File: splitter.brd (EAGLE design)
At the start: 23.8 x 17.8 mm, 16 parts

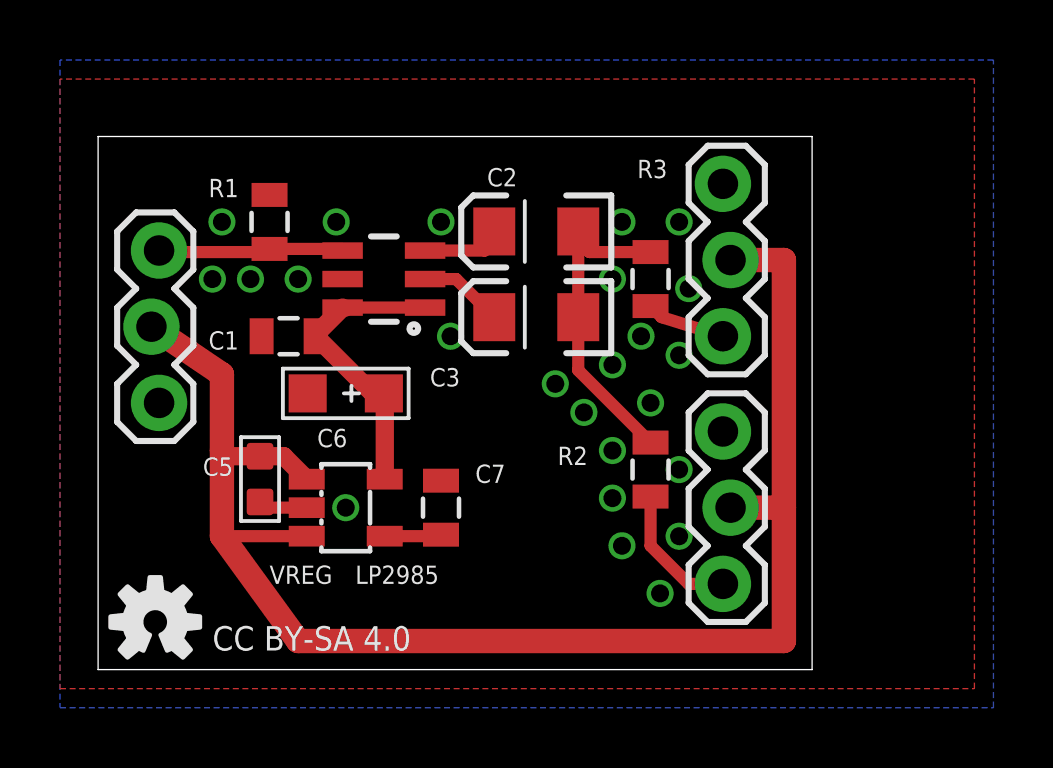
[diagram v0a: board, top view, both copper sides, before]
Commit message: Standardized the capacitors and increased their values for VREG IN/OUT
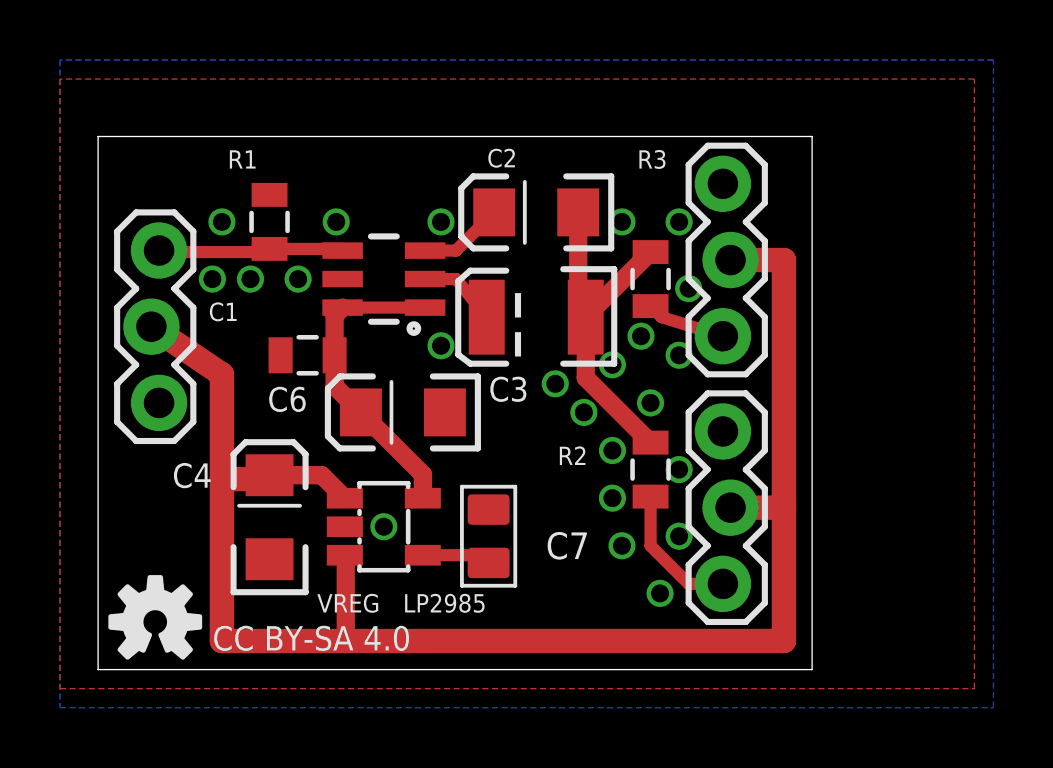
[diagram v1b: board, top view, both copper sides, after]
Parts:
- removed C5: 1uf, Seeed-OPL-Capacitor:C0603
- added C4: 22uf, SparkFun-Passives:EIA3216
- C3: value 100uF -> 100uf; device SparkFun-Passives:EIA3216 -> SparkFun-Passives:EIA3528
- C6: value 4.7uf -> 22uf; device Seeed-OPL-Capacitor:AVX-A -> SparkFun-Passives:EIA3216
- C7: device SparkFun-Passives:0805 -> Seeed-OPL-Capacitor:C0805
- moved C6 2.01 mm to (10.2, 8.57)
- moved C7 1.85 mm to (13.0, 4.45), turned to 0 degrees
- moved VREG 1.42 mm to (9.53, 4.76)
- moved C1 0.90 mm to (6.99, 10.5)
- moved C2 0.63 mm to (14.6, 15.2)
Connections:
- net 3.3V: now also C6.A; no longer C6.+
- net GND: now also C4.C, C6.C; no longer C5.2, C6.-
- net VCC: now also C4.A; no longer C5.1
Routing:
- net VCC: track 51.0 -> 54.1 mm
- net GND: track 1.64 -> 0.00 mm, vias 24 -> 23
- net N$7: track 10.9 -> 11.7 mm
